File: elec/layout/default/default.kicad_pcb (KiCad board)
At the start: 2 copper layers, 45 x 167 mm, 132 parts, among them U10 1kΩ ±1% 62.5mW, U11 1kΩ ±1% 62.5mW, U12 1kΩ ±1% 62.5mW, U13 1kΩ ±1% 62.5mW, U14 1kΩ ±1% 62.5mW, U15 1kΩ ±1% 62.5mW, U16 1kΩ ±1% 62.5mW, U17 1kΩ ±1% 62.5mW, U18 1kΩ ±1% 62.5mW, U7 1kΩ ±1% 62.5mW, U8 1kΩ ±1% 62.5mW, U9 1kΩ ±1% 62.5mW

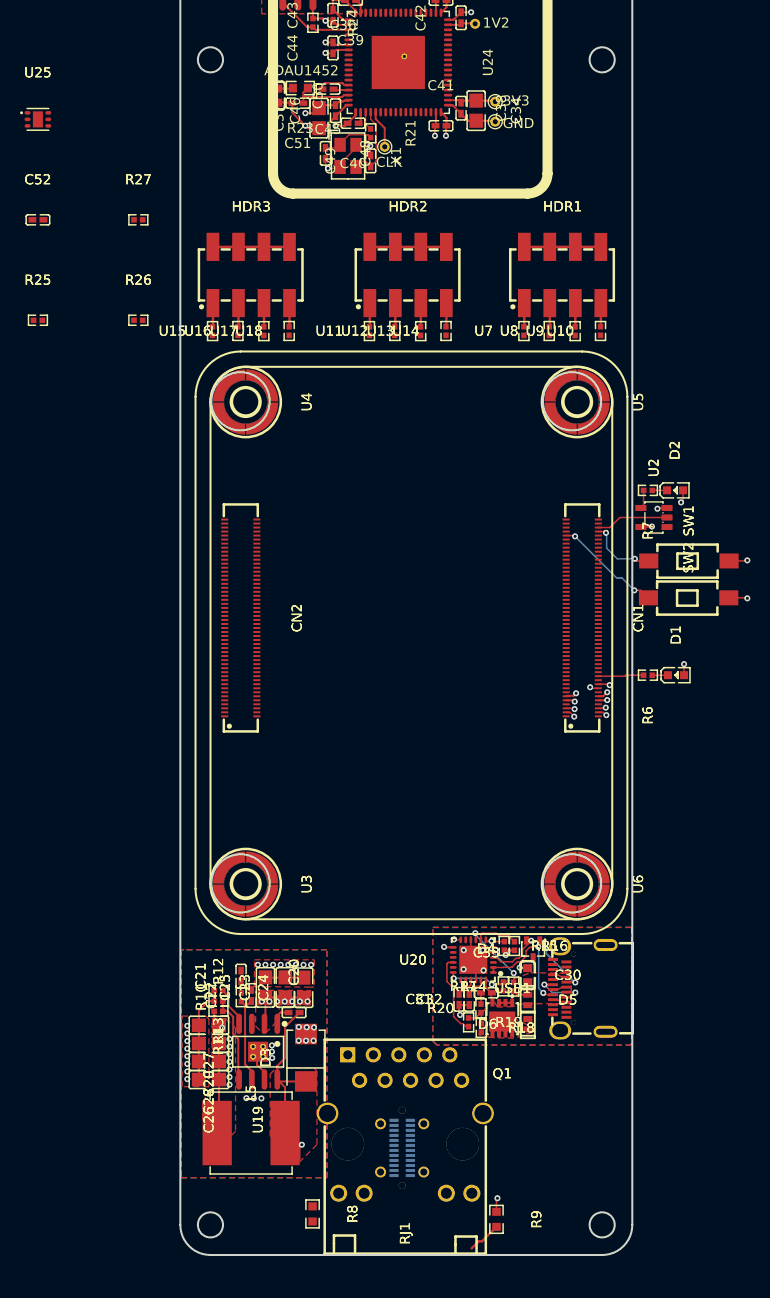
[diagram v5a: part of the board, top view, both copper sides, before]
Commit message: position connecotrs and regulator
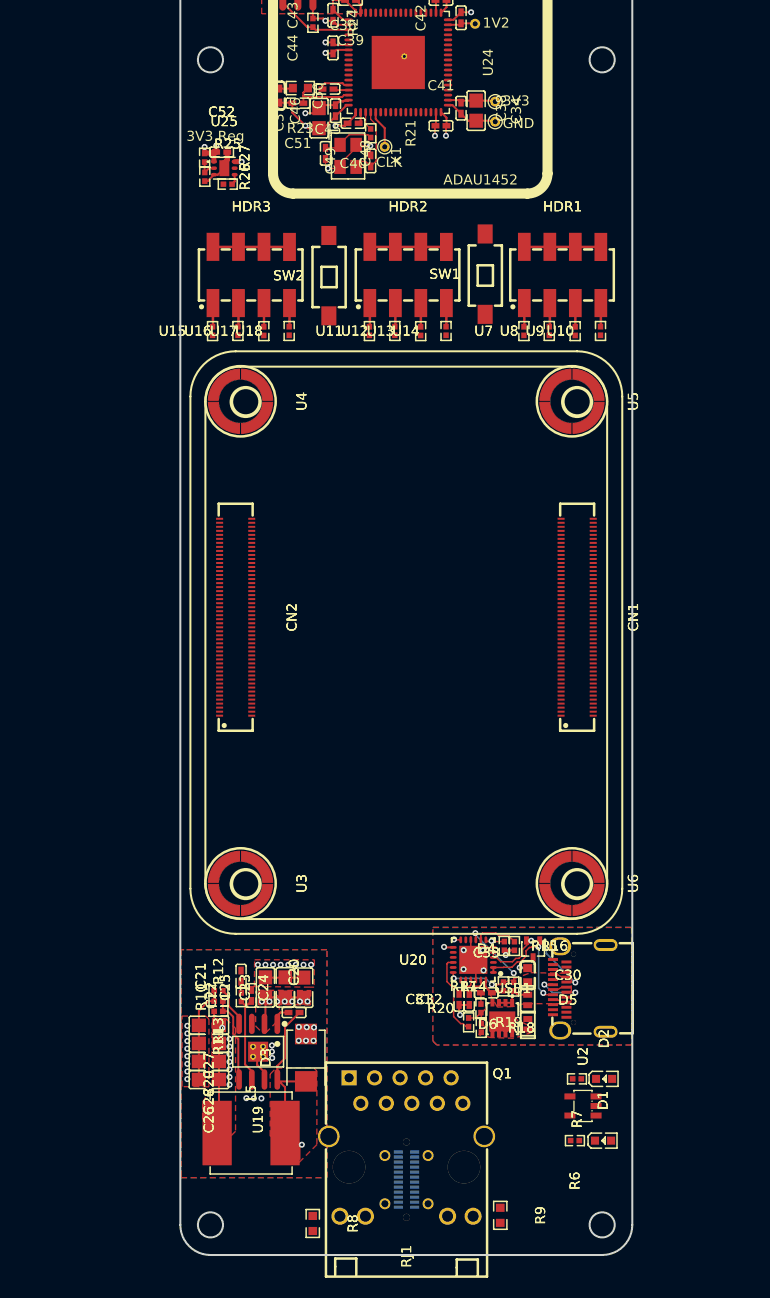
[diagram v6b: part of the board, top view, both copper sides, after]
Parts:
- moved D2 59.0 mm to (168.9, 172.5)
- moved R7 59.0 mm to (166.2, 172.5)
- moved U2 59.0 mm to (166.8, 175.2)
- moved SW2 48.1 mm to (141.5, 92.5), turned to 90 degrees
- moved R6 46.9 mm to (166.0, 178.7)
- moved D1 46.9 mm to (168.8, 178.7)
- moved SW1 35.0 mm to (157.0, 92.4), turned to 90 degrees
- moved R25 23.3 mm to (131.4, 83.4)
- moved C52 19.5 mm to (130.8, 80.2)
- moved U25 19.2 mm to (131.1, 81.9)
- moved R26 15.7 mm to (129.1, 82.7), turned to -90 degrees
- moved R27 9.04 mm to (129.1, 80.8), turned to -90 degrees
- moved U23 3.19 mm to (149.2, 182.6)
- moved RJ1 2.29 mm to (149.2, 179.3)
- moved R8 0.95 mm to (139.9, 186.9)
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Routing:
- net pins[91]: track 10.8 -> 0.00 mm, vias 2 -> 0
- net cm5.cm5-pins[94]: track 7.25 -> 0.00 mm
- net cm5-pins[92]: track 7.10 -> 0.00 mm, vias 2 -> 0
- net cm5.cm5-pins[20]: track 4.69 -> 0.00 mm
- net cm5.rj45-anode-1: track 3.36 -> 0.00 mm
- net regulator_3v3-FB: track 0.00 -> 2.13 mm
- net Y: track 1.86 -> 0.00 mm
- net cm5.cm5-cathode: track 1.57 -> 0.00 mm
- net cm5.cm5-cathode-1: track 1.47 -> 0.00 mm
- net hv: track 49.1 -> 47.8 mm, vias 12 -> 10
- net cm5-pins[16]: track 31.3 -> 30.1 mm, vias 1 -> 0
- net cm5-pins[11]: track 18.3 -> 17.2 mm, vias 1 -> 0
- net cm5-pins[10]: track 15.0 -> 14.0 mm, vias 1 -> 0
- net regulator_3v3-EN: track 0.00 -> 1.05 mm
- net cm5-pins[3]: track 19.0 -> 18.0 mm, vias 1 -> 0
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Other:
- outline, holes or cut-outs redrawn
- board text added: "3V3 Reg"
